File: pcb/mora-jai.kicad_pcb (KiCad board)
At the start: 2 copper layers, 150 x 150 mm, 108 parts, among them IC1 TPS61023DRLR, J1 Conn_01x02, J10 Conn_01x04, J2 Conn_01x04, J3 Conn_01x02, J4 Conn_01x03, J5 Conn_01x03, J6 Conn_01x02, J7 Conn_01x02, J8 Conn_01x02, Q1 Q_PMOS_DGS, SW1 SW_Push, SW10 SW_Push, SW11 SW_Push, SW12 SW_Push, SW13 SW_Push, SW14 SW_Push, SW15 SW_Push, SW16 SW_Push, SW2 SW_Push, SW3 SW_Push, SW4 SW_Push, SW5 SW_Push, SW6 SW_Push, SW7 SW_Push, SW8 SW_Push, SW9 SW_Push, U1 CD74HC4067M, U2 MCP73833-AMI-UN, U3 XIAO-ESP32-S3-SMD

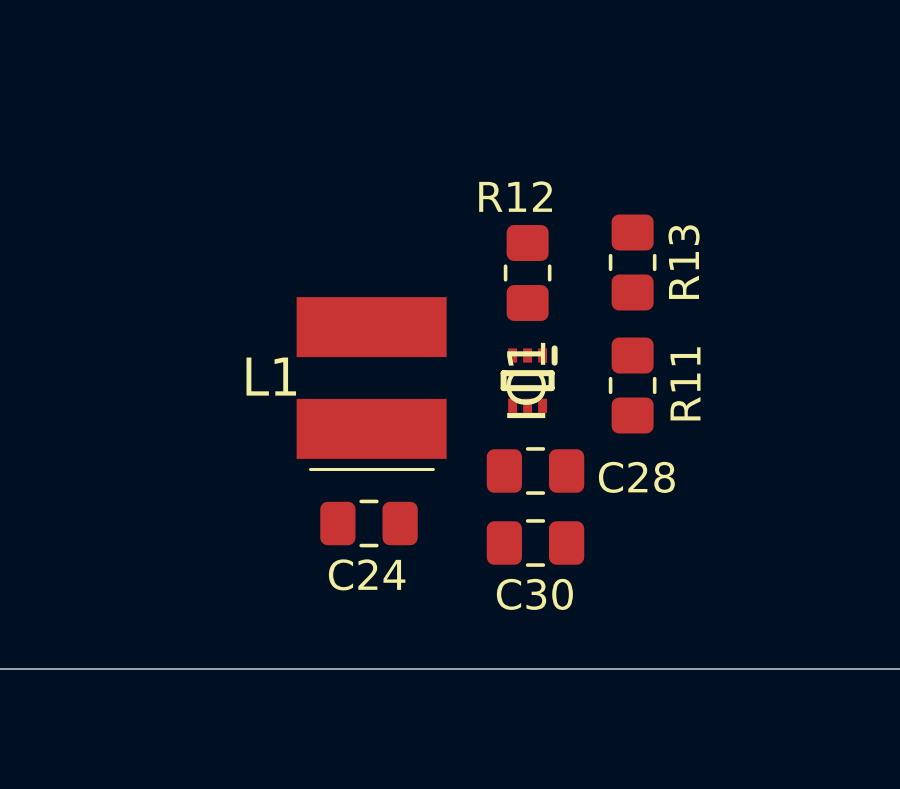
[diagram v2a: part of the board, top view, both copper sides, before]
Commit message: drew fill zones for 5V boost circuit
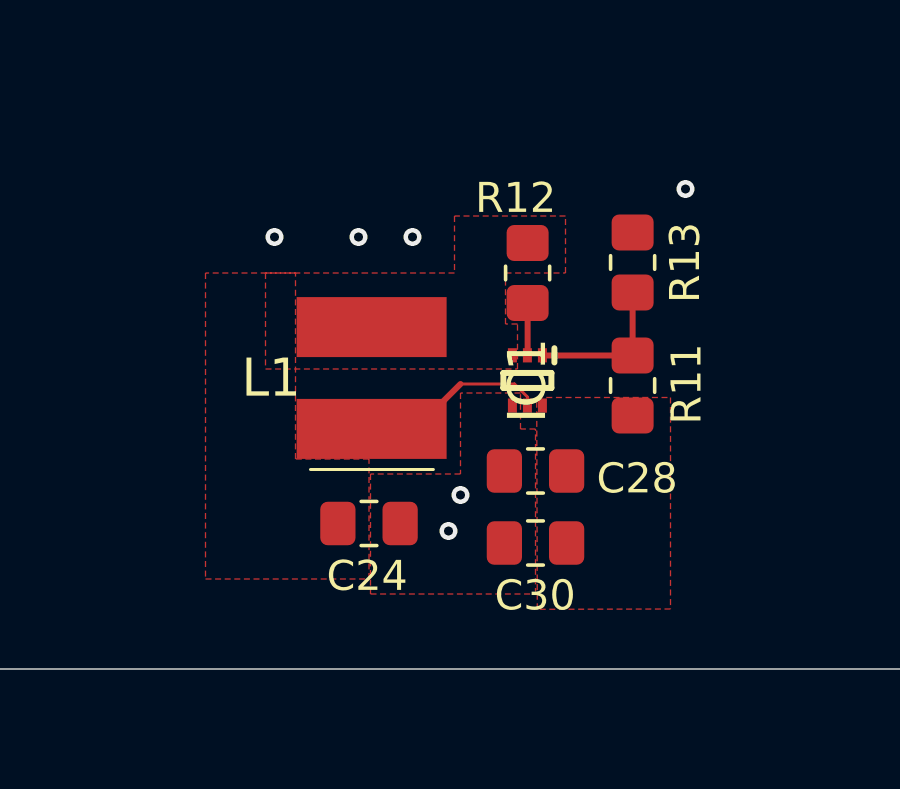
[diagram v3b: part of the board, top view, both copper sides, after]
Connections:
- U3 pad 20: unconnected-(U3-GND-Pad20) -> GND
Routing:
- net Net-(IC1-SW): track 0.00 -> 6.29 mm
- net Net-(IC1-FB): track 0.00 -> 5.10 mm
- net Net-(IC1-EN): track 0.00 -> 1.75 mm
- net GND: vias 31 -> 37
- added copper zone on F.Cu, net /Power/VIN
- added copper zone on F.Cu, net V_OUT
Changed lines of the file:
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@@
 		(capping no)
 		(filling no)
+		(zone_defaults)
 		(pcbplotparams
 			(layerselection 0x00000000_00000000_55555555_5755f5ff)
@@
 	(footprint "Mora_Jai_Parts:SOTFL50P160X60-6N"
 		(layer "F.Cu")
-		(at 142.2375 163.388 -90)
+		(at 142.23 163.382 -90)
 		(descr "SOT563 (6)")
 		(tags "Integrated Circuit")
@@
 		(sheetname "/Power/")
 		(sheetfile "power.kicad_sch")
-		(units
-			(unit
-				(name "A")
-				(pins "1" "2" "3" "4" "5" "6")
-			)
-		)
-		(attr smd)
+		(solder_mask_margin 0)
+		(clearance 0.2)
+		(attr smd allow_soldermask_bridges)
 		(duplicate_pad_numbers_are_jumpers no)
 		(fp_line
@@
 			(pinfunction "GND_4")
 			(pintype "passive")
+			(clearance 0.1)
 		)
 		(pad "5" smd rect
@@
 			(pinfunction "SW_5")
 			(pintype "passive")
+			(solder_mask_margin 0)
+			(solder_paste_margin 0)
+			(clearance 0.1)
 		)
 		(pad "6" smd rect
@@
 			(pinfunction "VOUT_6")
 			(pintype "passive")
+			(clearance 0.1)
 		)
 		(embedded_fonts no)
@@
 			(layers "*.Cu" "*.Mask")
 			(remove_unused_layers no)
-			(net "unconnected-(U3-GND-Pad20)")
+			(net "GND")
 			(pinfunction "GND_20")
-			(pintype "passive+no_connect")
+			(pintype "passive")
 		)
 		(pad "21" thru_hole circle
@@
 	)
 	(via
+		(at 147.5 157)
+		(size 0.6)
+		(drill 0.3)
+		(layers "F.Cu" "B.Cu")
+		(free yes)
+		(net "GND")
+	)
+	(via
 		(at 40.75 48.1)
 		(size 0.6)
@@
 	)
 	(via
+		(at 138.4 158.6)
+		(size 0.6)
+		(drill 0.3)
+		(layers "F.Cu" "B.Cu")
+		(free yes)
+		(net "GND")
+	)
+	(via
 		(at 51.3 30.1)
 		(size 0.6)
@@
 	)
 	(via
+		(at 139.6 168.4)
+		(size 0.6)
+		(drill 0.3)
+		(layers "F.Cu" "B.Cu")
+		(free yes)
+		(net "GND")
+	)
+	(via
 		(at 49.55 167.7)
 		(size 0.6)
@@
 	)
 	(via
+		(at 140 167.2)
+		(size 0.6)
+		(drill 0.3)
+		(layers "F.Cu" "B.Cu")
+		(free yes)
+		(net "GND")
+	)
+	(via
 		(at 87.85 128.7)
 		(size 0.6)
@@
 	)
 	(via
+		(at 133.8 158.6)
+		(size 0.6)
+		(drill 0.3)
+		(layers "F.Cu" "B.Cu")
+		(free yes)
+		(net "GND")
+	)
+	(via
+		(at 136.6 158.6)
+		(size 0.6)
+		(drill 0.3)
+		(layers "F.Cu" "B.Cu")
+		(free yes)
+		(net "GND")
+	)
+	(via
 		(at 122.55 82.25)
 		(size 0.6)
@@
 	)
 	(segment
+		(start 142.7375 162.55)
+		(end 145.7375 162.55)
+		(width 0.2)
+		(layer "F.Cu")
+		(net "Net-(IC1-FB)")
+	)
+	(segment
+		(start 145.7375 162.55)
+		(end 145.7375 160.45)
+		(width 0.2)
+		(layer "F.Cu")
+		(net "Net-(IC1-FB)")
+	)
+	(segment
 		(start 101 126.487501)
 		(end 105.2125 126.487501)
@@
 	)
 	(segment
+		(start 142.2375 163.9385)
+		(end 142.2375 164.226)
+		(width 0.1)
+		(layer "F.Cu")
+		(net "Net-(IC1-SW)")
+	)
+	(segment
+		(start 137.0375 164.997)
+		(end 138.503 164.997)
+		(width 0.2)
+		(layer "F.Cu")
+		(net "Net-(IC1-SW)")
+	)
+	(segment
+		(start 140 163.5)
+		(end 141.799 163.5)
+		(width 0.1)
+		(layer "F.Cu")
+		(net "Net-(IC1-SW)")
+	)
+	(segment
+		(start 138.503 164.997)
+		(end 140 163.5)
+		(width 0.2)
+		(layer "F.Cu")
+		(net "Net-(IC1-SW)")
+	)
+	(segment
+		(start 141.799 163.5)
+		(end 142.2375 163.9385)
+		(width 0.1)
+		(layer "F.Cu")
+		(net "Net-(IC1-SW)")
+	)
+	(segment
 		(start 53.3 139.3)
 		(end 55 141)
@@
 	)
 	(segment
+		(start 142.2375 162.55)
+		(end 142.2375 160.8)
+		(width 0.2)
+		(layer "F.Cu")
+		(net "Net-(IC1-EN)")
+	)
+	(segment
 		(start 97.75 137.750001)
 		(end 104.25 137.750001)
@@
 	)
 	(segment
+		(start 36.165 83.701363)
+		(end 36 83.536363)
+		(width 0.5)
+		(layer "F.Cu")
+		(net "ESPBAT")
+	)
+	(segment
 		(start 105.5 65.5)
 		(end 97.5 65.5)
@@
 		(net "Net-(D3-DOUT)")
 	)
-	(segment
-		(start 36.165 83.701363)
-		(end 36 83.536363)
-		(width 0.5)
+	(zone
+		(net "/Power/VIN")
 		(layer "F.Cu")
-		(net "ESPBAT")
+		(hatch edge 0.5)
+		(priority 3)
+		(connect_pads yes
+			(clearance 0)
+		)
+		(min_thickness 0.25)
+		(fill yes
+			(thermal_gap 0)
+			(thermal_bridge_width 0.5)
+			(smoothing chamfer)
+			(island_removal_mode 0)
+		)
+		(polygon
+			(pts
+				(xy 134.5 159.8) (xy 131.5 159.8) (xy 131.5 170) (xy 136.95 170) (xy 136.95 166) (xy 134.5 166)
+			)
+		)
+	)
+	(zone
+		(net "GND")
+		(layer "F.Cu")
+		(hatch edge 0.5)
+		(priority 4)
+		(connect_pads yes
+			(clearance 0)
+		)
+		(min_thickness 0.25)
+		(fill yes
+			(thermal_gap 0)
+			(thermal_bridge_width 0.5)
+			(smoothing chamfer)
+			(island_removal_mode 0)
+		)
+		(polygon
+			(pts
+				(xy 137 166.5) (xy 137 170.5) (xy 142.5 170.5) (xy 142.5 165) (xy 142 165) (xy 142 163.8) (xy 140 163.8)
+				(xy 140 166.5)
+			)
+		)
+	)
+	(zone
+		(net "/Power/VIN")
+		(layer "F.Cu")
+		(hatch edge 0.5)
+		(priority 1)
+		(connect_pads yes
+			(clearance 0)
+		)
+		(min_thickness 0.25)
+		(fill yes
+			(thermal_gap 0.5)
+			(thermal_bridge_width 0.5)
+			(smoothing chamfer)
+			(island_removal_mode 0)
+		)
+		(polygon
+			(pts
+				(xy 133.5 159.8) (xy 133.5 163) (xy 141.9 163) (xy 141.9 161.5) (xy 141.5 161.5) (xy 141.5 159.8)
+				(xy 143.5 159.8) (xy 143.5 157.9) (xy 139.8 157.9) (xy 139.8 159.8) (xy 136.9 159.8)
+			)
+		)
+	)
+	(zone
+		(net "V_OUT")
+		(layer "F.Cu")
+		(hatch edge 0.5)
+		(priority 2)
+		(connect_pads yes
+			(clearance 0)
+		)
+		(min_thickness 0.1)
+		(fill yes
+			(thermal_gap 0)
+			(thermal_bridge_width 0.5)
+			(smoothing chamfer)
+			(island_removal_mode 0)
+		)
+		(polygon
+			(pts
+				(xy 142.54 163.95) (xy 147 163.95) (xy 147 171) (xy 142.56 171.01)
+			)
+		)
 	)
 	(zone
@@
 	)
 	(group ""
-		(members "0aa58446-1149-4e1b-b4f2-fd62b2f055f5" "307b58ff-9ce7-4adb-8c76-a6ed7f27a334"
-			"412ad251-343d-48b6-a05f-4392f6e3b00a" "50076768-7adc-4684-b620-b44bf6cc551d"
-			"5df82e8e-1f75-40f9-bc86-d64893822cc1" "6c4fef53-4fad-4cfe-8fa0-ca846189ff55"
-			"bf4414c5-a7dc-44e0-87de-db29243f906e" "c0f1a1c8-ea72-42b0-b5da-986181e0a6fc"
+		(members "0aa58446-1149-4e1b-b4f2-fd62b2f055f5" "0eaec98f-88fd-401d-bdcb-352d22a3928c"
+			"307b58ff-9ce7-4adb-8c76-a6ed7f27a334" "412ad251-343d-48b6-a05f-4392f6e3b00a"
+			"50076768-7adc-4684-b620-b44bf6cc551d" "5df82e8e-1f75-40f9-bc86-d64893822cc1"
+			"6acb6c1c-d5a5-4800-a528-10e9b30b6653" "6c4fef53-4fad-4cfe-8fa0-ca846189ff55"
+			"bdf1eff2-a2fd-4a93-b231-73762ebaef05" "bf4414c5-a7dc-44e0-87de-db29243f906e"
+			"c0f1a1c8-ea72-42b0-b5da-986181e0a6fc"
 		)
 	)

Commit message: drew fill zones for battery charger
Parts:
- moved C24 4.00 mm to (132.9, 168.2)
- moved C28 4.00 mm to (138.5, 166.4)
- moved C30 4.00 mm to (138.5, 168.8)
- moved IC1 4.00 mm to (138.2, 163.4)
- moved L1 4.00 mm to (133.0, 163.3)
- moved R11 4.00 mm to (141.7, 163.6)
- moved R12 4.00 mm to (138.2, 159.8)
- moved R13 4.00 mm to (141.7, 159.4)
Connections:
- net /Power/VIN renamed VIN
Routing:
- net ~{STAT1}: track 0.00 -> 57.6 mm, vias 0 -> 4
- net ~{STAT2}: track 0.00 -> 56.8 mm, vias 0 -> 1
- net ~{PWR_GOOD}: track 0.00 -> 39.9 mm, vias 0 -> 1
- net VIN: track 0.00 -> 39.5 mm
- net +BATT: track 0.00 -> 25.6 mm, vias 0 -> 7
- net +3V3: track 159.7 -> 181.2 mm
- net Net-(U2-PROG): track 0.00 -> 3.96 mm
- net Net-(U2-THERM): track 0.00 -> 3.15 mm
- net VBUS: vias 0 -> 4
- net GND: vias 37 -> 58
- added copper zone on B.Cu, net +BATT
- added copper zone on F.Cu, net +BATT
- added copper zone on B.Cu, net VBUS
- added copper zone on F.Cu, net VBUS

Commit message: finished revision 2
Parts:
- moved TP2 6.43 mm to (62.3, 77.3)
- moved TP3 6.43 mm to (66.9, 81.8)
- moved R9 1.80 mm to (40.0, 96.0)
- moved R3 1.50 mm to (36.0, 96.0)
- moved S1 0.80 mm to (28.4, 58.1)
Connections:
- JP2 pad 1: OLED_PWR -> +3V3
- JP2 pad 2: +3V3 -> OLED_PWR
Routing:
- net V_OUT: track 22.9 -> 257.4 mm, vias 3 -> 6
- net ~{STAT2}: track 56.8 -> 209.1 mm, vias 1 -> 7
- net ~{PWR_GOOD}: track 39.9 -> 189.6 mm, vias 1 -> 5
- net /SW_12: track 22.0 -> 161.7 mm, vias 2 -> 5
- net VBUS: track 0.00 -> 134.2 mm
- net +BATT: track 25.6 -> 158.0 mm, vias 7 -> 10
- net ~{STAT1}: track 57.6 -> 187.0 mm, vias 4 -> 10
- net Net-(D12-DOUT): track 20.8 -> 145.5 mm, vias 0 -> 4
- net +3V3: track 181.2 -> 302.9 mm, vias 4 -> 5
- net VIN: track 39.5 -> 120.8 mm
- net +5V: track 967.6 -> 887.9 mm, vias 19 -> 20
- net Net-(D11-DOUT): track 143.3 -> 218.1 mm, vias 3 -> 10
- net Net-(D10-DIN): track 120.6 -> 194.2 mm, vias 0 -> 6
- net USB_D-: track 0.00 -> 71.0 mm, vias 0 -> 3
- net USB_D+: track 0.00 -> 70.2 mm, vias 0 -> 3
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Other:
- board text added: "+3V3 GND"
- board text added: "+5V PWR +3V3"
- board text added: "CHIP_EN"
- board text added: "D10"
- board text added: "D8"
- board text added: "ESPBAT"
- board text added: "GND ESPBAT"
- board text added: "MTCK"
- board text added: "MTDO"
- board text added: "MTDO MTDI GND CHIP_EN MTCK MTMS USBD+ USBD-"
- board text added: "Open Mora Jai Box PCB rev. 2 PCB+FW by: Alec Bargher CAD Model by: Eren Slifker Software by: Isaac Berman Emotional Support: shmoopy"
- board text added: "Power debug pins"
- board text added: "VBUS USB_D+ USB_D- GND"
- board text added: "VIN GND"
- board text added: "V_OUT GND"
- board text added: "~{PWR_GOOD} ~{STAT2} ~{STAT1}"
- board text removed: "+5V +3V3 PWR"
- board text removed: "Open Mora Jai Box PCB rev. 1 PCB+FW by: Alec Bargher CAD Model by: Eren Slifker Software by: Isaac Berman Emotional Support: shmoopy"
- board text removed: "TODO: - Route fill traces for battery charger & boost circuits"
